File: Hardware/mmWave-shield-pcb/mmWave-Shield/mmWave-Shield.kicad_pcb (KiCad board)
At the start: 2 copper layers, 31 parts, among them J3 DF40HC_3.0_-40DS-0.4V_51, J4 DF40HC_3.0_-50DS-0.4V_51, J5 DF40C-40DP-0.4V_51, J6 DF40C-50DP-0.4V_51, U1 KC2016K80.0000C1GE00

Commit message: kicad project inital version
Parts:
- FB1, FB2, FB3, FB4, FB5, FB6, FB7: footprint Inductor_SMD:L_01005_0402Metric -> MMZ1005S121CT000:IND_1005_TDK-L
- J5: footprint Connector_Hirose_DF40:Hirose_DF40HC(3.0)-40DS-0.4V_2x20_P0.4mm -> Connector_Hirose_DF40:Hirose_DF40C-40DS-0.4V_2x20_P0.4mm
- J6: footprint Connector_Hirose_DF40:Hirose_DF40HC(3.0)-50DS-0.4V_2x25_P0.4mm -> Connector_Hirose_DF40:Hirose_DF40C-50DS-0.4V_2x25_P0.4mm
- moved J3 20.4 mm to (112.7, 74.8)
- moved J5 20.4 mm to (112.7, 81.0)
- moved J6 20.4 mm to (113.7, 68.7)
- moved J4 20.4 mm to (113.7, 62.6)

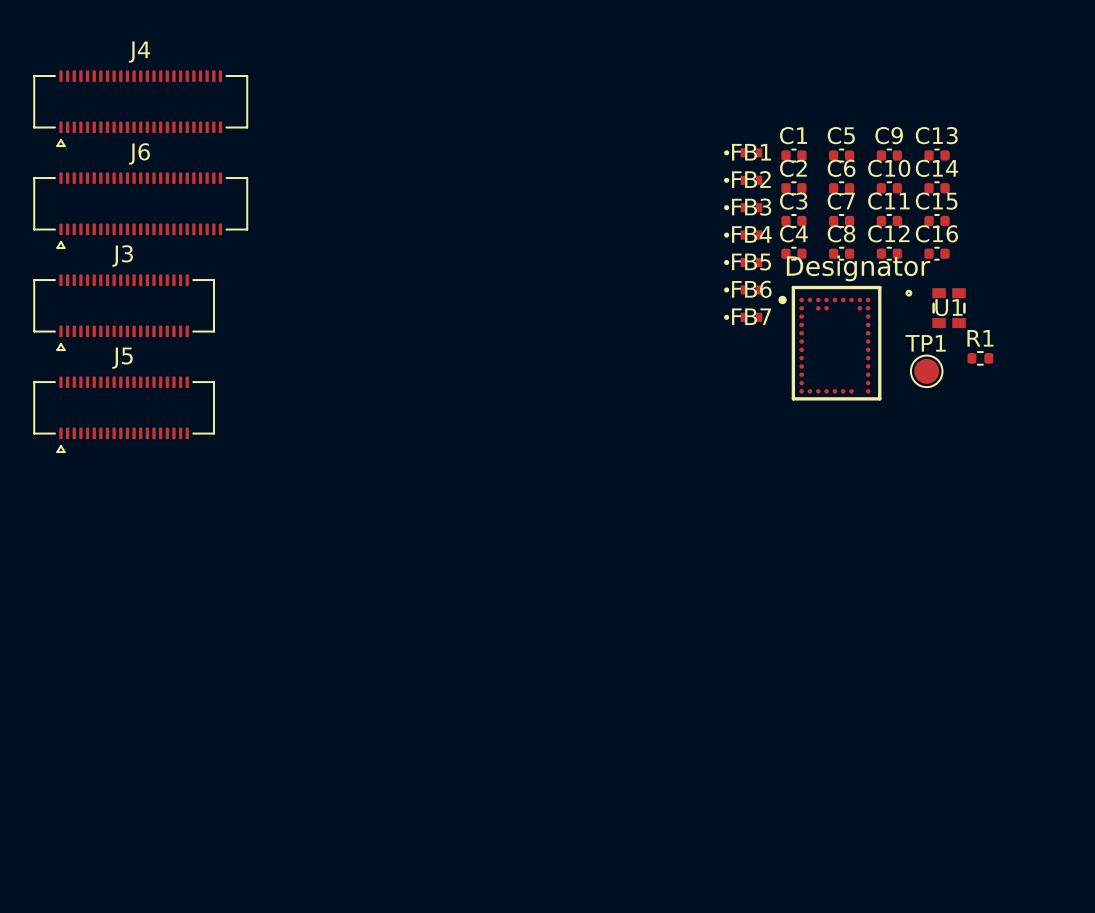
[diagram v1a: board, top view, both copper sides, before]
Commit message: arranged components on pcb
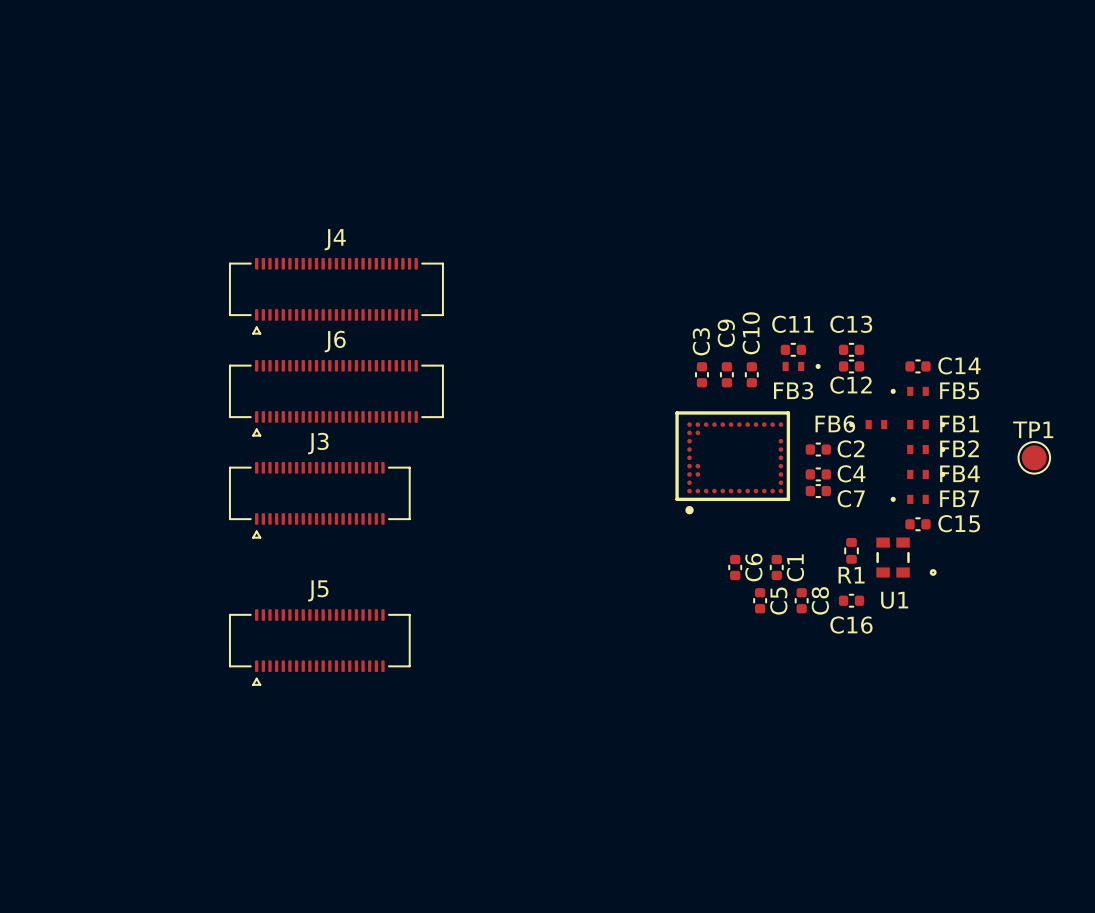
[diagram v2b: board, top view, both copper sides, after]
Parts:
- moved C5 27.2 mm to (151.0, 92.6), turned to -90 degrees
- moved C1 24.8 mm to (152.0, 90.6), turned to -90 degrees
- moved C6 23.7 mm to (149.5, 90.6), turned to -90 degrees
- moved C16 21.5 mm to (156.5, 92.6)
- moved C8 21.0 mm to (153.5, 92.6), turned to -90 degrees
- moved FB1 19.2 mm to (160.5, 82.0), turned to 180 degrees
- moved FB2 19.1 mm to (160.5, 83.5), turned to 180 degrees
- moved J5 18.3 mm to (124.5, 95.0)
- moved C15 18.3 mm to (160.5, 88.0)
- moved FB4 17.6 mm to (160.5, 85.0), turned to 180 degrees
- moved C9 16.4 mm to (149.0, 79.0), turned to 90 degrees
- moved J3 16.3 mm to (124.5, 86.1)
- moved J6 16.3 mm to (125.5, 80.0)
- moved J4 16.3 mm to (125.5, 73.9)
- moved C7 16.3 mm to (154.5, 86.0)
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
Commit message: working on scematic1
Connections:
- net /Connectors/ADS_A_DR renamed ADS_A_DR
- net /Connectors/ADS_B_DR renamed ADS_B_DR
- net /Connectors/CSI_CLK_N renamed CSI_CLK_N
- net /Connectors/CSI_CLK_P renamed CSI_CLK_P
- net /Connectors/CSI_D0_N renamed CSI_D0_N
- net /Connectors/CSI_D0_P renamed CSI_D0_P
- net /Connectors/I2C_A_SCL renamed I2C_A_SCL
- net /Connectors/I2C_A_SDA renamed I2C_A_SDA
- net /Connectors/I2C_B_SCL renamed I2C_B_SCL
- net /Connectors/I2C_B_SDA renamed I2C_B_SDA
- net /Connectors/MIC_CLK renamed MIC_CLK
- net /Connectors/MIC_DATA renamed MIC_DATA
- net /Connectors/MIC_THSEL renamed MIC_THSEL
- net /Connectors/MIC_WAKE renamed MIC_WAKE
- net /Connectors/MSP_CS renamed nRF_P0.25
- net /Connectors/MSP_DR1 renamed nRF_P0.26
- net /Connectors/MSP_DR2 renamed nRF_P0.27
- net /Connectors/MSP_TCK renamed MSP_TCK
- net /Connectors/MSP_TDI renamed MSP_TDI
- net /Connectors/MSP_TDO renamed MSP_TDO
- net /Connectors/MSP_TMS renamed MSP_TMS
- net /Connectors/MSP_VCC renamed MSP_VCC
- net /Connectors/MSP_~{TRST} renamed MSP_~{TRST}
- net /Connectors/SPI_B_CLK renamed SPI_B_CLK
- net /Connectors/SPI_B_CS renamed SPI_B_CS
- net /Connectors/SPI_B_MISO renamed SPI_B_MISO
- net /Connectors/SPI_B_MOSI renamed SPI_B_MOSI
- net /Connectors/SWDCLK renamed SWDCLK
- net /Connectors/SWDIO renamed SWDIO
- net /Connectors/SWO renamed SWO
- net /Connectors/nRF_P0.31 renamed nRF_P0.31
- net /Connectors/nRF_P1.09_GAP_GPIO62 renamed nRF_P1.09_GAP_GPIO62
- net /Connectors/nRF_P1.11_GAP_GPIO63 renamed nRF_P1.11_GAP_GPIO63
- net /Connectors/nRF_P1.12_GAP_GPIO64 renamed nRF_P1.12_GAP_GPIO64
- net /Connectors/~{RST} renamed ~{RST}
- C14 pad 2: VD1 -> VD2
- FB5 pad 1: VD1 -> VD2
- J3 pad 20: /Connectors/nRF_P0.04 -> nRF_P0.04
- J3 pad 22: /Connectors/nRF_P0.05 -> nRF_P0.05
- J3 pad 26: /Connectors/nRF_P0.07 -> nRF_P0.07
- J5 pad 19: /Connectors/nRF_P0.04 -> nRF_P0.04
- J5 pad 21: /Connectors/nRF_P0.05 -> nRF_P0.05
- J5 pad 25: /Connectors/nRF_P0.07 -> nRF_P0.07
- U$1 pad C1: nRF_P1.01_GAP_GPIO61 -> nRF_P0.05
- U$1 pad F1: /sensor/RST -> nRF_P0.04
- U$1 pad G1: SPI_A_CS -> nRF_P0.07

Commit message: Placed Connectors in hopefully right way
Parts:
- removed J5: DF40C-40DP-0.4V_51, Connector_Hirose_DF40:Hirose_DF40C-40DS-0.4V_2x20_P0.4mm
- removed J6: DF40C-50DP-0.4V_51, Connector_Hirose_DF40:Hirose_DF40C-50DS-0.4V_2x25_P0.4mm
- J3, J4: moved to B.Cu
- moved J3 33.5 mm to (155.0, 100.0), turned to -90 degrees
- moved J4 29.8 mm to (139.6, 100.1), turned to 90 degrees
- moved TP1 19.3 mm to (151.6, 94.9)
- moved C11 18.7 mm to (143.2, 93.4)
- moved C12 18.7 mm to (146.7, 94.4)
- moved C13 18.7 mm to (146.7, 93.4)
- moved FB3 18.7 mm to (143.2, 94.4)
- moved C10 18.1 mm to (140.8, 94.3)
- moved C3 18.1 mm to (137.8, 94.3)
- moved C9 18.1 mm to (139.3, 94.3)
- moved C14 17.2 mm to (155.2, 94.9)
- moved C15 17.2 mm to (155.2, 104.4)
- moved FB1 17.2 mm to (155.2, 98.4)
- moved FB2 17.2 mm to (155.2, 99.9)
- moved FB4 17.2 mm to (155.2, 101.4)
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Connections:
- net nRF_P0.07 renamed nRF_P0.07/AMUX
- J3 pad 1: /Connectors/RESET_N -> RESET_N
- J3 pad 11: /Connectors/TDO -> TDO
- J3 pad 13: /Connectors/VCC_GAP9 -> VCC_GAP9
- J3 pad 14: /Connectors/VQPS_FUSE_1V8 -> VQPS_FUSE_1V8
- J3 pad 16: /Connectors/QVAR_IMU_1 -> QVAR_IMU_1
- J3 pad 18: /Connectors/QVAR_IMU_2 -> QVAR_IMU_2
- J3 pad 29: /Connectors/GAP_GPIO46 -> GAP_GPIO46
- J3 pad 3: /Connectors/~{TRST} -> ~{TRST}
- J3 pad 31: /Connectors/GAP_GPIO47 -> GAP_GPIO47
- J3 pad 33: /Connectors/GAP_GPIO50 -> GAP_GPIO50
- J3 pad 35: /Connectors/GAP_GPIO51 -> GAP_GPIO51
- J3 pad 37: /Connectors/GAP_GPIO48 -> GAP_GPIO48
- J3 pad 39: /Connectors/GAP_GPIO49 -> GAP_GPIO49
- J3 pad 5: /Connectors/TCK -> TCK
- J3 pad 7: /Connectors/TCS/CS_RAM_GATE -> TCS/CS_RAM_GATE
- J3 pad 9: /Connectors/TDI -> TDI
- J4 pad 23: nRF_P0.25 -> MSP_CS
- J4 pad 25: nRF_P0.26 -> MSP_DR1
- J4 pad 27: /Connectors/nRF_QSPI_CS_CONN -> nRF_QSPI_CS_CONN
- J4 pad 29: /Connectors/nRF_QSPI_IO3 -> nRF_QSPI_IO3
- J4 pad 31: /Connectors/nRF_QSPI_IO2 -> nRF_QSPI_IO2
- J4 pad 33: /Connectors/nRF_QSPI_IO1 -> nRF_QSPI_IO1
- J4 pad 37: /Connectors/nRF_QSPI_IO0 -> nRF_QSPI_IO0
- J4 pad 39: /Connectors/nRF_QSPI_CLK -> nRF_QSPI_CLK
- J4 pad 41: nRF_P0.27 -> MSP_DR2
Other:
- board outline added: 21 x 15 mm
- board text added: "MICWAKE"
- board text added: "SPI_B_MOSI"
- board text added: "VBAT"
- board text added: "connectors center to center: X Distance 15.4mm Y Distance 0.1mm (according to Baseboard Altium PCB design)"
- board text added: "nrf_P0.31"

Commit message: V1 of pcb layout
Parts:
- C16: value 1uF -> 10nF
- TP1: footprint TestPoint:TestPoint_Pad_D1.5mm -> TestPoint:TestPoint_Pad_D1.0mm
- moved C3 7.32 mm to (145.1, 95.3)
- moved C9 6.92 mm to (146.2, 95.3)
- moved C10 6.52 mm to (147.3, 95.3)
- moved FB3 6.32 mm to (149.4, 95.8)
- moved C11 6.31 mm to (149.4, 94.7)
- moved C12 4.98 mm to (151.5, 95.8)
- moved C13 4.95 mm to (151.5, 94.7)
- moved C6 4.92 mm to (146.0, 103.8)
- moved C5 4.78 mm to (147.1, 103.8)
- moved C1 4.65 mm to (148.2, 103.8)
- moved C8 4.50 mm to (149.3, 103.8)
- moved C15 2.99 mm to (153.6, 101.8)
- moved FB7 2.83 mm to (153.6, 100.5)
- moved TP1 2.72 mm to (150.0, 97.1)
- moved FB4 2.43 mm to (153.6, 99.5)
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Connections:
- J3 pad 1: RESET_N -> unconnected-(J3-Pad1)
- J3 pad 11: TDO -> unconnected-(J3-Pad11)
- J3 pad 12: nRF_P1.12_GAP_GPIO64 -> nRF_P0.12_GAP_GPIO64
- J3 pad 13: VCC_GAP9 -> unconnected-(J3-Pad13)
- J3 pad 14: VQPS_FUSE_1V8 -> unconnected-(J3-Pad14)
- J3 pad 16: QVAR_IMU_1 -> unconnected-(J3-Pad16)
- J3 pad 17: CSI_CLK_N -> unconnected-(J3-Pad17)
- J3 pad 18: QVAR_IMU_2 -> unconnected-(J3-Pad18)
- J3 pad 19: CSI_CLK_P -> unconnected-(J3-Pad19)
- J3 pad 2: nRF_P0.31 -> unconnected-(J3-Pad2)
- J3 pad 20: nRF_P0.04 -> GAP_GPIO46
- J3 pad 22: nRF_P0.05 -> unconnected-(J3-Pad22)
- J3 pad 23: CSI_D0_N -> unconnected-(J3-Pad23)
- J3 pad 25: CSI_D0_P -> unconnected-(J3-Pad25)
- J3 pad 26: nRF_P0.07/AMUX -> unconnected-(J3-Pad26)
- J3 pad 3: ~{TRST} -> unconnected-(J3-Pad3)
- J3 pad 31: GAP_GPIO47 -> unconnected-(J3-Pad31)
- J3 pad 33: GAP_GPIO50 -> unconnected-(J3-Pad33)
- J3 pad 34: MIC_DATA -> unconnected-(J3-Pad34)
- J3 pad 35: GAP_GPIO51 -> unconnected-(J3-Pad35)
- J3 pad 36: MIC_CLK -> unconnected-(J3-Pad36)
- J3 pad 37: GAP_GPIO48 -> unconnected-(J3-Pad37)
- J3 pad 38: MIC_THSEL -> unconnected-(J3-Pad38)
- J3 pad 39: GAP_GPIO49 -> unconnected-(J3-Pad39)
- J3 pad 4: nRF_P1.00_GAP_GPIO60 -> unconnected-(J3-Pad4)
- J3 pad 40: MIC_WAKE -> unconnected-(J3-Pad40)
- J3 pad 5: TCK -> unconnected-(J3-Pad5)
- J3 pad 6: nRF_P1.01_GAP_GPIO61 -> unconnected-(J3-Pad6)
- J3 pad 7: TCS/CS_RAM_GATE -> unconnected-(J3-Pad7)
- J3 pad 8: nRF_P1.09_GAP_GPIO62 -> unconnected-(J3-Pad8)
- J3 pad 9: TDI -> unconnected-(J3-Pad9)
- J4 pad 1: VBAT -> unconnected-(J4-Pad1)
- J4 pad 10: SWDIO -> unconnected-(J4-Pad10)
- J4 pad 12: SWDCLK -> unconnected-(J4-Pad12)
- J4 pad 14: SWO -> unconnected-(J4-Pad14)
- J4 pad 17: VD1 -> unconnected-(J4-Pad17)
- J4 pad 18: VD0 -> unconnected-(J4-Pad18)
- J4 pad 2: MSP_~{TRST} -> unconnected-(J4-Pad2)
- J4 pad 20: VA0 -> unconnected-(J4-Pad20)
- J4 pad 21: VA1 -> unconnected-(J4-Pad21)
- J4 pad 22: MSP_TMS -> unconnected-(J4-Pad22)
- J4 pad 23: MSP_CS -> unconnected-(J4-Pad23)
- J4 pad 24: MSP_TDI -> unconnected-(J4-Pad24)
- J4 pad 25: MSP_DR1 -> unconnected-(J4-Pad25)
- J4 pad 26: MSP_TDO -> unconnected-(J4-Pad26)
- J4 pad 27: nRF_QSPI_CS_CONN -> unconnected-(J4-Pad27)
- J4 pad 28: MSP_VCC -> unconnected-(J4-Pad28)
- J4 pad 29: nRF_QSPI_IO3 -> unconnected-(J4-Pad29)
- J4 pad 3: VBAT -> unconnected-(J4-Pad3)
- J4 pad 30: I2C_A_SCL -> unconnected-(J4-Pad30)
- J4 pad 31: nRF_QSPI_IO2 -> unconnected-(J4-Pad31)
- J4 pad 32: I2C_A_SDA -> unconnected-(J4-Pad32)
- J4 pad 33: nRF_QSPI_IO1 -> unconnected-(J4-Pad33)
- J4 pad 37: nRF_QSPI_IO0 -> unconnected-(J4-Pad37)
- J4 pad 38: I2C_B_SDA -> unconnected-(J4-Pad38)
- J4 pad 39: nRF_QSPI_CLK -> unconnected-(J4-Pad39)
- J4 pad 4: MSP_TCK -> unconnected-(J4-Pad4)
- J4 pad 41: MSP_DR2 -> unconnected-(J4-Pad41)
- J4 pad 42: I2C_B_SCL -> unconnected-(J4-Pad42)
- J4 pad 43: ADS_A_DR -> unconnected-(J4-Pad43)
- J4 pad 45: ADS_B_DR -> unconnected-(J4-Pad45)
- J4 pad 46: SPI_A_CS -> unconnected-(J4-Pad46)
- J4 pad 47: SPI_B_CS -> unconnected-(J4-Pad47)
- J4 pad 48: SPI_B_CLK -> unconnected-(J4-Pad48)
- J4 pad 49: SPI_B_MOSI -> unconnected-(J4-Pad49)
- J4 pad 5: VSYS -> unconnected-(J4-Pad5)
- J4 pad 50: SPI_B_MISO -> unconnected-(J4-Pad50)
- J4 pad 6: /Connectors/EXT_CHG/VUSB -> unconnected-(J4-Pad6)
- J4 pad 7: VSYS -> unconnected-(J4-Pad7)
- J4 pad 8: /Connectors/EXT_CHG/VUSB -> unconnected-(J4-Pad8)
- J4 pad 9: ~{RST} -> unconnected-(J4-Pad9)
- U$1 pad C1: nRF_P0.05 -> nRF_P0.12_GAP_GPIO64
- U$1 pad F1: nRF_P0.04 -> GAP_GPIO46
- U$1 pad G1: nRF_P0.07/AMUX -> nRF_P1.11_GAP_GPIO63
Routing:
- net GND: track 0.00 -> 35.3 mm, vias 0 -> 34
- net 1V8: track 0.00 -> 29.1 mm, vias 0 -> 4
- net VD2: track 0.00 -> 18.1 mm, vias 0 -> 2
- net VDD_RF: track 0.00 -> 16.7 mm, vias 0 -> 4
- net nRF_P1.11_GAP_GPIO63: track 0.00 -> 15.0 mm, vias 0 -> 1
- net GAP_GPIO46: track 0.00 -> 14.8 mm, vias 0 -> 1
- net VDD_A: track 0.00 -> 14.0 mm, vias 0 -> 2
- net nRF_P0.12_GAP_GPIO64: track 0.00 -> 11.4 mm, vias 0 -> 1
- net VDD_LF: track 0.00 -> 10.3 mm, vias 0 -> 2
- net VDD_D: track 0.00 -> 10.2 mm, vias 0 -> 2
- net SPI_A_MISO: track 0.00 -> 9.07 mm, vias 0 -> 1
- net SPI_A_MOSI: track 0.00 -> 9.07 mm, vias 0 -> 1
- net SPI_A_CLK: track 0.00 -> 9.04 mm, vias 0 -> 1
- net Net-(C15--): track 0.00 -> 8.40 mm
- net VDD_PLL: track 0.00 -> 5.86 mm, vias 0 -> 2
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- added copper zone on B.Cu, net GND
- added copper zone on F.Cu, net GND
- added copper zone on In1.Cu, net GND
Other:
- copper layers 2 -> 4
- board text added: "BioGAP"
- board text added: "BoardOutline? Because connector close to edge"
- board text added: "mmWave shield"

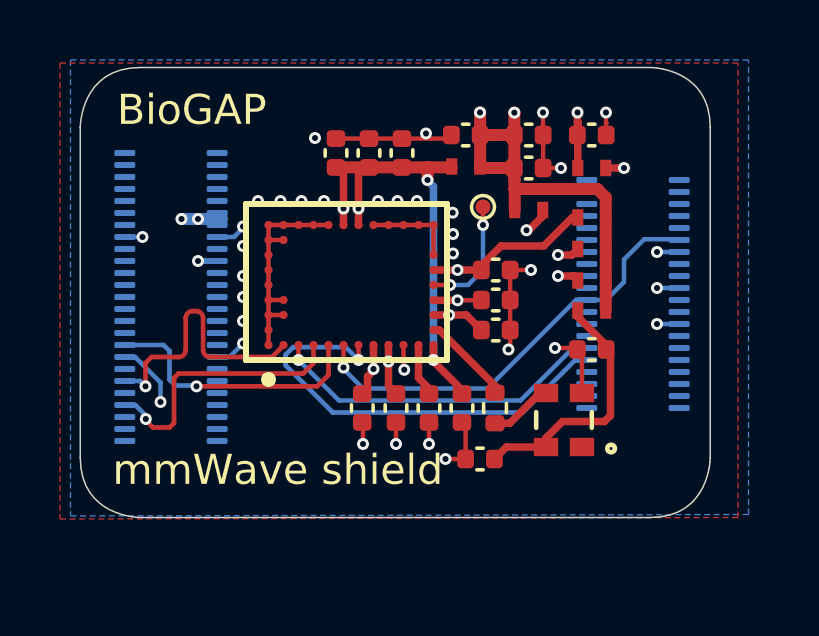
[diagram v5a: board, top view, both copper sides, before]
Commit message: added some docs fpr the pcb
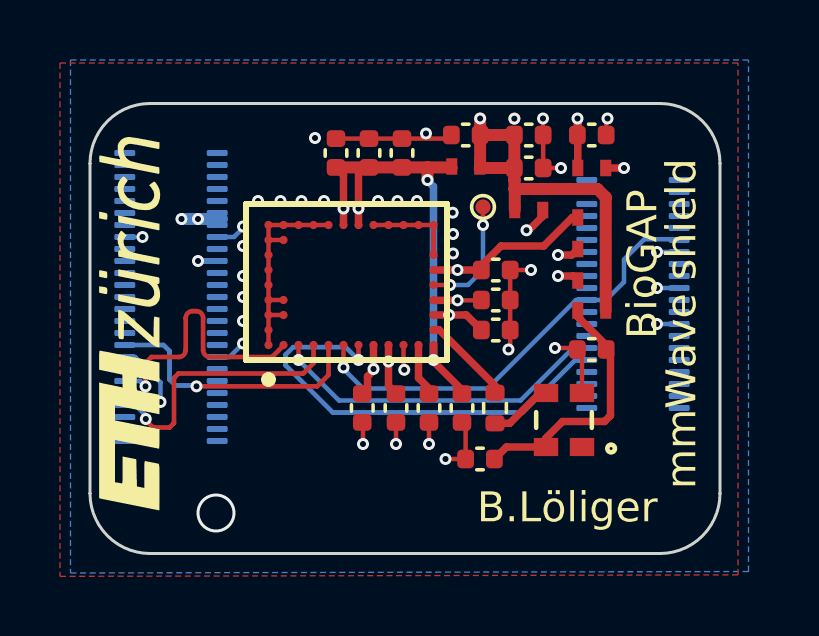
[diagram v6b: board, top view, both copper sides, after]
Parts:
- added REF**: LOGO, dz_art:ETH_zurich_2mm, F.Cu at (138.2, 101.0)
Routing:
- net 1V8: track 29.1 -> 28.1 mm
- net (no net): vias 0 -> 1
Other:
- board text added: "B.Löliger"

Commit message: small adjustments
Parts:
- added R3: 0ohm, Resistor_SMD:R_0805_2012Metric, F.Cu at (130.5, 83.8)
- added R4: 0ohm, Resistor_SMD:R_0805_2012Metric, F.Cu at (130.5, 86.8)
- added U1: TPS22916CYFPR, aaEXTRAS:TPS22916CYFPR, F.Cu at (134.8, 83.2)
- added U2: TPS22916CYFPR, aaEXTRAS:TPS22916CYFPR, F.Cu at (134.8, 85.6)
- moved C1 1.45 mm to (148.2, 105.2)
- moved C14 1.45 mm to (153.7, 96.2)
- moved C15 1.45 mm to (153.7, 103.3)
- moved C3 1.45 mm to (145.2, 96.8)
- moved C5 1.45 mm to (147.2, 105.2)
- moved C6 1.45 mm to (146.0, 105.2)
- moved C9 1.45 mm to (146.2, 96.8)
- moved DIV 1.45 mm to (150.1, 98.5)
- moved FB1 1.45 mm to (153.7, 98.9)
- moved FB2 1.45 mm to (153.7, 100.0)
- moved FB4 1.45 mm to (153.7, 101.0)
- moved FB5 1.45 mm to (153.7, 97.2)
- moved FB7 1.45 mm to (153.7, 102.0)
- moved U$1 1.45 mm to (145.7, 101.2)
- moved X1 1.45 mm to (152.8, 105.7)
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- renumbered TP1 to DIV, U1 to X1
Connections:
- C14 pad 2: VD2 -> 3V3
- FB5 pad 1: VD2 -> 3V3
- J3 pad 26: unconnected-(J3-Pad26) -> nRF_P0.07/AMUX
- J4 pad 11: 1V8 -> 1V8_Connector
- J4 pad 13: 1V8 -> 1V8_Connector
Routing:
- net VD2: track 18.1 -> 0.00 mm, vias 2 -> 0
- net 1V8: track 28.1 -> 13.4 mm, vias 4 -> 2
- net nRF_P1.11_GAP_GPIO63: track 15.0 -> 0.50 mm
- net VDD_A: track 14.0 -> 2.54 mm
- net nRF_P0.12_GAP_GPIO64: track 11.4 -> 0.50 mm
- net GAP_GPIO46: track 14.8 -> 5.12 mm
- net VDD_LF: track 10.3 -> 2.41 mm
- net VDD_D: track 10.2 -> 2.50 mm
- net GND: track 34.9 -> 28.2 mm, vias 34 -> 27
- net VDD_RF: track 16.7 -> 10.6 mm
- net VDD_PLL: track 5.86 -> 2.55 mm
- net /sensor/DIV_OUT: track 3.96 -> 1.15 mm, vias 2 -> 4
- net 3V3: track 0.00 -> 2.31 mm, vias 0 -> 1
- net SPI_A_CLK: track 9.04 -> 10.9 mm, vias 1 -> 0
- net SPI_A_MOSI: track 9.07 -> 10.5 mm, vias 1 -> 0
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- added copper zone on In2.Cu, net 1V8
- added copper zone on In2.Cu, net GND
- added copper zone on In2.Cu, net VD2
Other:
- board text added: "E-P H-P"
